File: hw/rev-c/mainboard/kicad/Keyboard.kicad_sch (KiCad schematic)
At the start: 7 parts, among them J15 KEYBOARD_EX, J5 KEYBOARD, U19 74LS145

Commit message: hw: fix wire/grid violations in schematic
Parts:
- J5: symbol Retrocomputing:CBM_PET_Keyboard_Conn_Keyed_20P -> EconoPET:CBM_PET_Keyboard_Conn_Keyed_20P
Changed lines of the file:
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@@
 	)
 	(symbol
-		(lib_id "Retrocomputing:CBM_PET_Keyboard_Conn_Keyed_20P")
+		(lib_id "EconoPET:CBM_PET_Keyboard_Conn_Keyed_20P")
 		(at 201.93 73.66 180)
 		(unit 1)

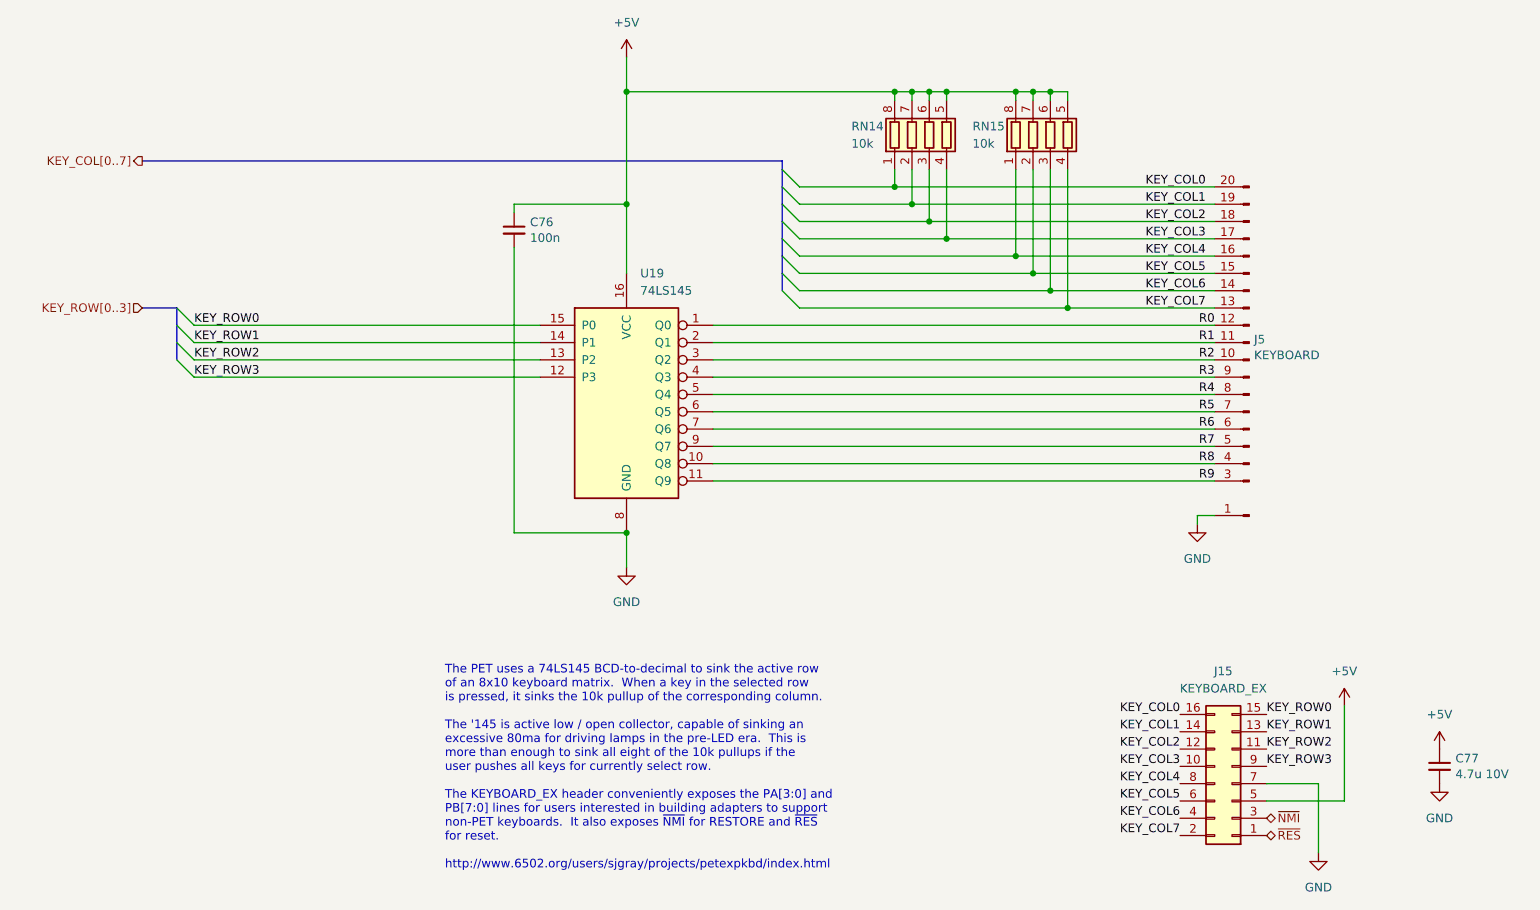
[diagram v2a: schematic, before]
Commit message: hw: renumber reference designators
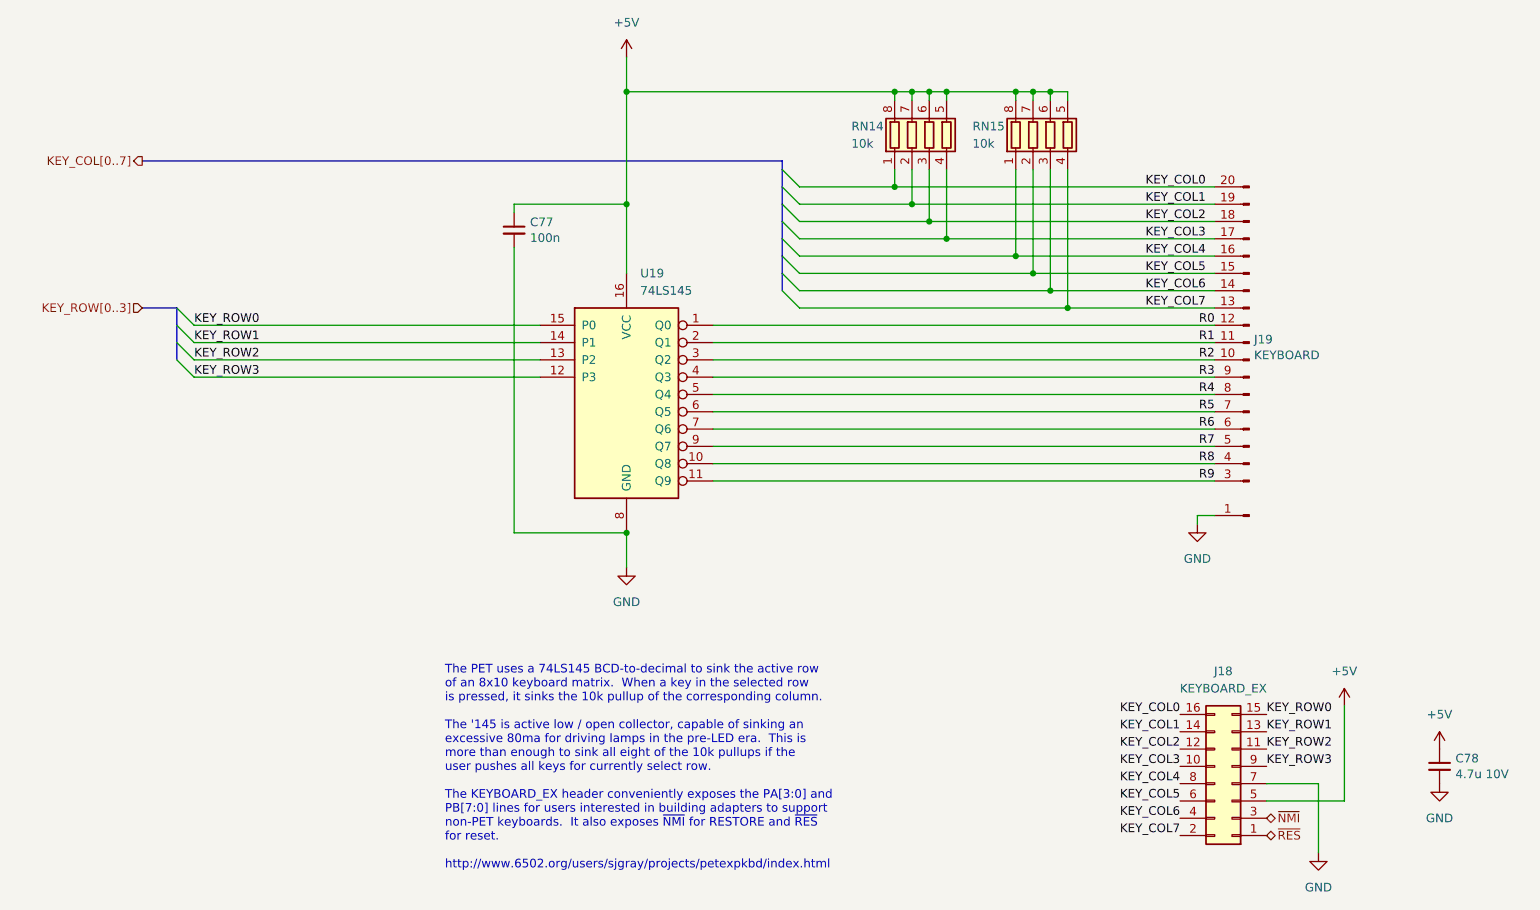
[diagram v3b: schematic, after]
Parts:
- renumbered C76 to C77, C77 to C78, J15 to J18, J5 to J19
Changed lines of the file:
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@@
 		(on_board yes)
 		(dnp no)
-		(property "Reference" "J5"
+		(property "Reference" "J19"
 			(at 202.6412 70.6628 0)
 			(effects
@@
 			(project ""
 				(path "/2eea20e6-112c-411a-b615-885ae773135a/00000000-0000-0000-0000-000061a7d9c6"
-					(reference "J5")
+					(reference "J19")
 					(unit 1)
 				)
@@
 		(on_board yes)
 		(dnp no)
-		(property "Reference" "C76"
+		(property "Reference" "C77"
 			(at 96.3168 53.4416 0)
 			(effects
@@
 			(project ""
 				(path "/2eea20e6-112c-411a-b615-885ae773135a/00000000-0000-0000-0000-000061a7d9c6"
-					(reference "C76")
+					(reference "C77")
 					(unit 1)
 				)
@@
 		(dnp no)
 		(fields_autoplaced yes)
-		(property "Reference" "#PWR0180"
+		(property "Reference" "#PWR0139"
 			(at 215.9 128.27 0)
 			(effects
@@
 			(project ""
 				(path "/2eea20e6-112c-411a-b615-885ae773135a/00000000-0000-0000-0000-000061a7d9c6"
-					(reference "#PWR0180")
+					(reference "#PWR0139")
 					(unit 1)
 				)
@@
 		(dnp no)
 		(fields_autoplaced yes)
-		(property "Reference" "J15"
+		(property "Reference" "J18"
 			(at 198.12 119.38 0)
 			(effects
@@
 			(project ""
 				(path "/2eea20e6-112c-411a-b615-885ae773135a/00000000-0000-0000-0000-000061a7d9c6"
-					(reference "J15")
+					(reference "J18")
 					(unit 1)
 				)
@@
 		(dnp no)
 		(fields_autoplaced yes)
-		(property "Reference" "#PWR0138"
+		(property "Reference" "#PWR0140"
 			(at 229.87 134.62 0)
 			(effects
@@
 			(project ""
 				(path "/2eea20e6-112c-411a-b615-885ae773135a/00000000-0000-0000-0000-000061a7d9c6"
-					(reference "#PWR0138")
+					(reference "#PWR0140")
 					(unit 1)
 				)
@@
 		(on_board yes)
 		(dnp no)
-		(property "Reference" "C77"
+		(property "Reference" "C78"
 			(at 232.2068 132.1816 0)
 			(effects
@@
 			(project ""
 				(path "/2eea20e6-112c-411a-b615-885ae773135a/00000000-0000-0000-0000-000061a7d9c6"
-					(reference "C77")
+					(reference "C78")
 					(unit 1)
 				)
@@
 		(dnp no)
 		(fields_autoplaced yes)
-		(property "Reference" "#PWR0179"
+		(property "Reference" "#PWR0138"
 			(at 212.09 152.4 0)
 			(effects
@@
 			(project ""
 				(path "/2eea20e6-112c-411a-b615-885ae773135a/00000000-0000-0000-0000-000061a7d9c6"
-					(reference "#PWR0179")
+					(reference "#PWR0138")
 					(unit 1)
 				)
@@
 		(dnp no)
 		(fields_autoplaced yes)
-		(property "Reference" "#PWR0139"
+		(property "Reference" "#PWR0141"
 			(at 229.87 142.24 0)
 			(effects
@@
 			(project ""
 				(path "/2eea20e6-112c-411a-b615-885ae773135a/00000000-0000-0000-0000-000061a7d9c6"
-					(reference "#PWR0139")
-					(unit 1)
-				)
+					(reference "#PWR0141")
+					(unit 1)
+				)

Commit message: hw: match original PET designators for connectors
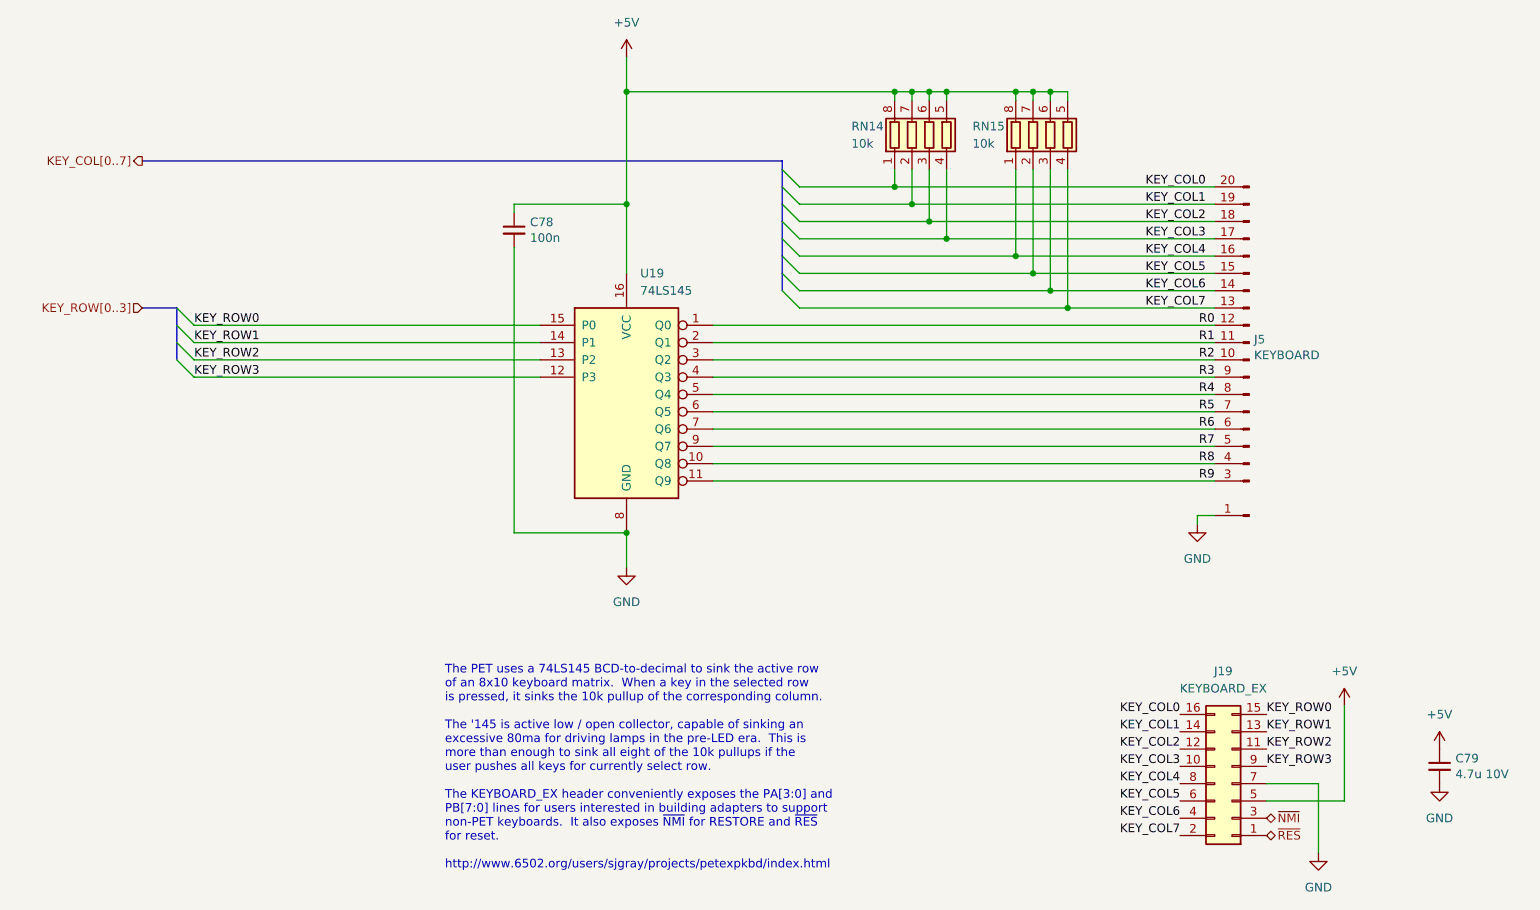
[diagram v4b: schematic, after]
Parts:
- renumbered C77 to C78, C78 to C79, J18 to J19, J19 to J5
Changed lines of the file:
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@@
 		(on_board yes)
 		(dnp no)
-		(property "Reference" "J19"
+		(property "Reference" "J5"
 			(at 202.6412 70.6628 0)
 			(effects
@@
 			(project ""
 				(path "/2eea20e6-112c-411a-b615-885ae773135a/00000000-0000-0000-0000-000061a7d9c6"
-					(reference "J19")
+					(reference "J5")
 					(unit 1)
 				)
@@
 		(on_board yes)
 		(dnp no)
-		(property "Reference" "C77"
+		(property "Reference" "C78"
 			(at 96.3168 53.4416 0)
 			(effects
@@
 			(project ""
 				(path "/2eea20e6-112c-411a-b615-885ae773135a/00000000-0000-0000-0000-000061a7d9c6"
-					(reference "C77")
+					(reference "C78")
 					(unit 1)
 				)
@@
 		(dnp no)
 		(fields_autoplaced yes)
-		(property "Reference" "J18"
+		(property "Reference" "J19"
 			(at 198.12 119.38 0)
 			(effects
@@
 			(project ""
 				(path "/2eea20e6-112c-411a-b615-885ae773135a/00000000-0000-0000-0000-000061a7d9c6"
-					(reference "J18")
+					(reference "J19")
 					(unit 1)
 				)
@@
 		(on_board yes)
 		(dnp no)
-		(property "Reference" "C78"
+		(property "Reference" "C79"
 			(at 232.2068 132.1816 0)
 			(effects
@@
 			(project ""
 				(path "/2eea20e6-112c-411a-b615-885ae773135a/00000000-0000-0000-0000-000061a7d9c6"
-					(reference "C78")
-					(unit 1)
-				)
+					(reference "C79")
+					(unit 1)
+				)

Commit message: hw: tidy warnings
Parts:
- J5: footprint Retrocomputing:CBM_PET_KEYBOARD_KEYED_20P -> EconoPET:CBM_PET_KEYBOARD_KEYED_20P
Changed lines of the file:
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@@
 			)
 		)
-		(property "Footprint" "Retrocomputing:CBM_PET_KEYBOARD_KEYED_20P"
+		(property "Footprint" "EconoPET:CBM_PET_KEYBOARD_KEYED_20P"
 			(at 201.93 73.66 0)
 			(effects

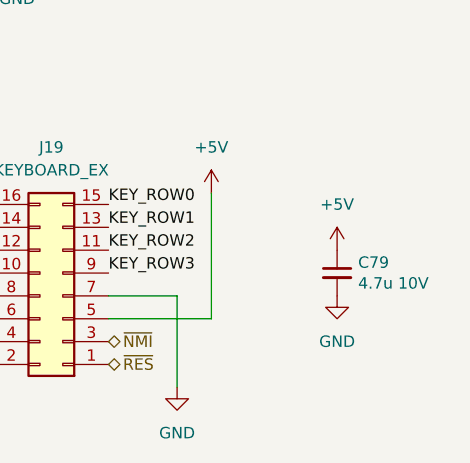
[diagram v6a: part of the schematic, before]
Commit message: hw: routing touchups, killer poke mitigation
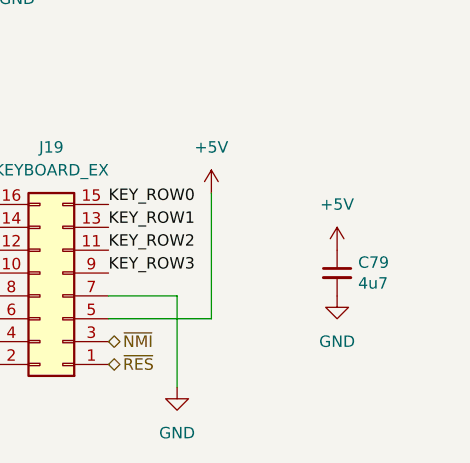
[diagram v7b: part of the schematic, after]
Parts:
- C79: value 4.7u 10V -> 4u7; LCSC C23733 -> C1538
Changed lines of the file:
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@@
 			)
 		)
-		(property "Value" "4.7u 10V"
+		(property "Value" "4u7"
 			(at 232.2068 134.493 0)
 			(effects
@@
 			)
 		)
-		(property "Datasheet" "https://product.samsungsem.com/mlcc/CL05A475MP5NRN.do"
+		(property "Datasheet" "https://www.lcsc.com/datasheet/lcsc_datasheet_2304140030_FH--Guangdong-Fenghua-Advanced-Tech-0402B472K500NT_C1538.pdf"
 			(at 229.87 133.35 0)
 			(effects
@@
 			)
 		)
-		(property "LCSC" "C23733"
+		(property "LCSC" "C1538"
 			(at 229.87 133.35 0)
 			(effects

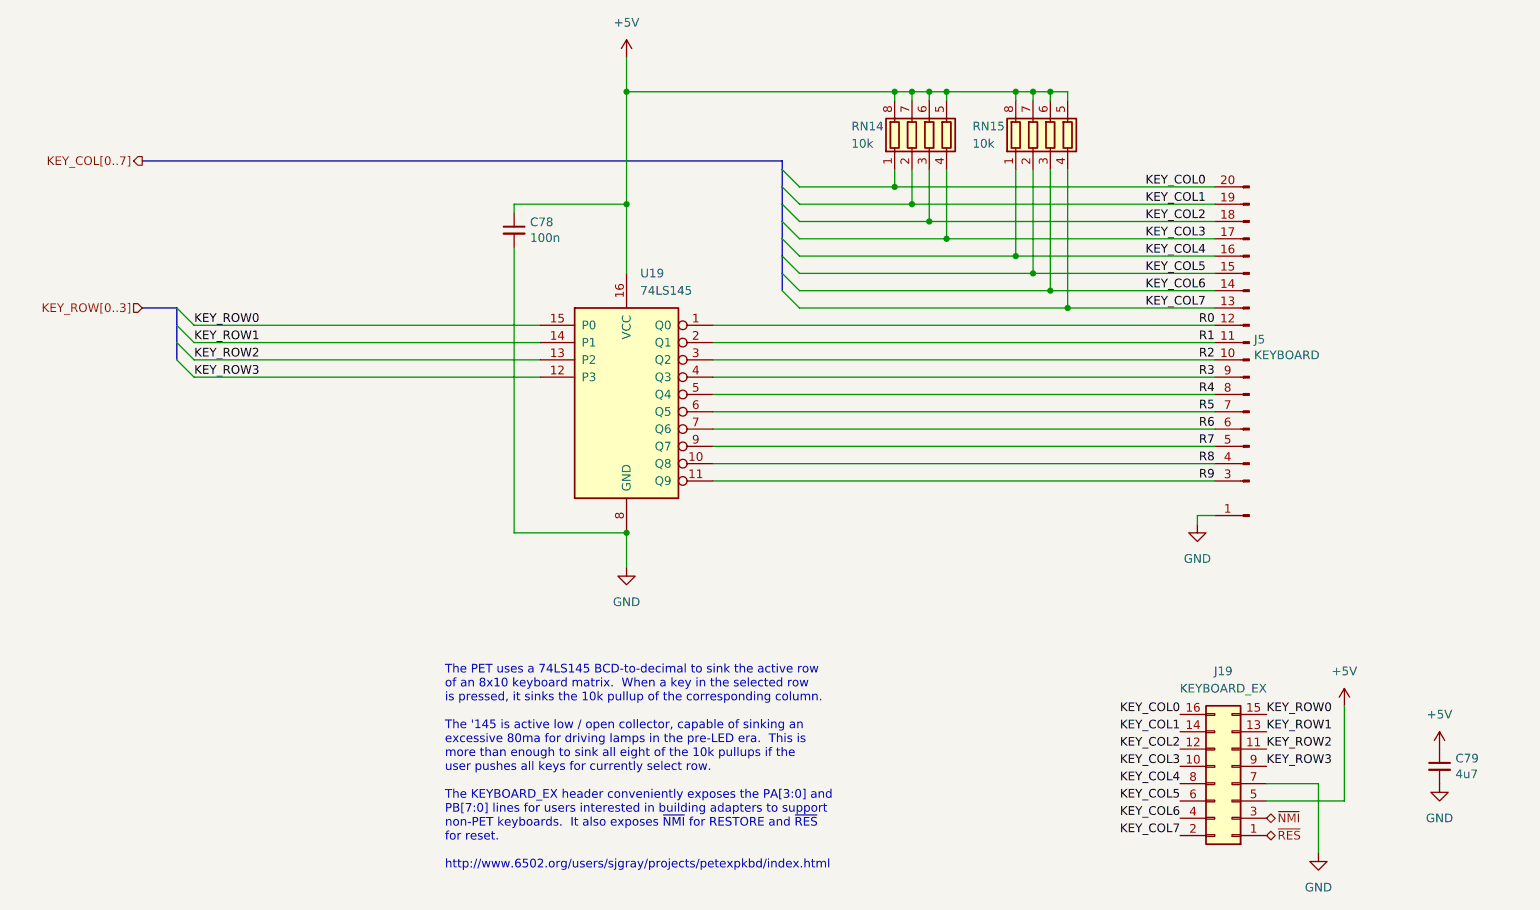
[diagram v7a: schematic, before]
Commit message: hw: fix/update parts / use parallel resistors to control 5V
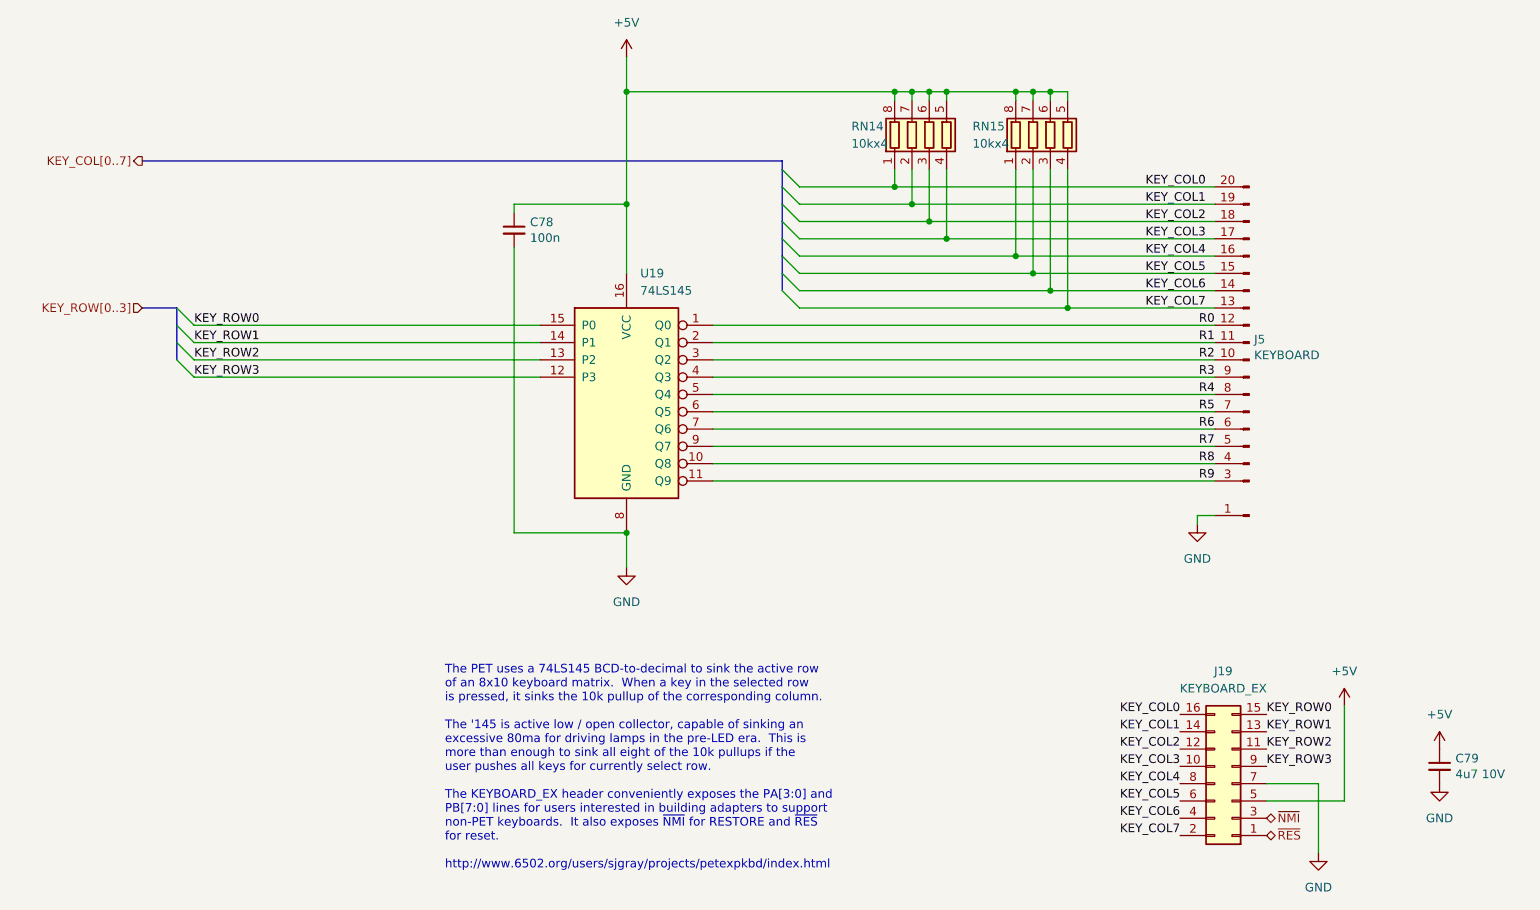
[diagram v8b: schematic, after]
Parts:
- C79: value 4u7 -> 4u7 10V; LCSC C1538 -> C23733
- RN14, RN15: value 10k -> 10kx4
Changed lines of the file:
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@@
 			)
 		)
-		(property "Datasheet" "https://datasheet.lcsc.com/lcsc/2304140030_Samsung-Electro-Mechanics-CL05B104KB54PNC_C307331.pdf"
+		(property "Datasheet" "https://product.samsungsem.com/mlcc/CL05B104KB54PN.do"
 			(at 93.98 54.61 0)
 			(effects
@@
 			)
 		)
-		(property "Datasheet" "https://datasheet.lcsc.com/lcsc/1809051911_Texas-Instruments-SN74LS145DR_C60829.pdf"
+		(property "Datasheet" "https://www.lcsc.com/datasheet/lcsc_datasheet_1809051911_Texas-Instruments-SN74LS145DR_C60829.pdf"
 			(at 110.49 78.74 0)
 			(effects
@@
 			)
 		)
-		(property "Value" "4u7"
+		(property "Value" "4u7 10V"
 			(at 232.2068 134.493 0)
 			(effects
@@
 			)
 		)
-		(property "Datasheet" "https://www.lcsc.com/datasheet/lcsc_datasheet_2304140030_FH--Guangdong-Fenghua-Advanced-Tech-0402B472K500NT_C1538.pdf"
+		(property "Datasheet" "https://product.samsungsem.com/mlcc/CL05A475MP5NRN.do"
 			(at 229.87 133.35 0)
 			(effects
@@
 			)
 		)
-		(property "LCSC" "C1538"
+		(property "LCSC" "C23733"
 			(at 229.87 133.35 0)
 			(effects
@@
 			)
 		)
-		(property "Value" "10k"
+		(property "Value" "10kx4"
 			(at 143.51 41.91 0)
 			(effects
@@
 			)
 		)
-		(property "Datasheet" "https://datasheet.lcsc.com/lcsc/2304140030_UNI-ROYAL-Uniroyal-Elec-4D03WGJ0103T5E_C29718.pdf"
+		(property "Datasheet" "https://www.lcsc.com/datasheet/lcsc_datasheet_2304140030_UNI-ROYAL-Uniroyal-Elec-4D03WGJ0103T5E_C29718.pdf"
 			(at 154.94 40.64 0)
 			(effects
@@
 			)
 		)
-		(property "Value" "10k"
+		(property "Value" "10kx4"
 			(at 161.29 41.91 0)
 			(effects
@@
 			)
 		)
-		(property "Datasheet" "https://datasheet.lcsc.com/lcsc/2304140030_UNI-ROYAL-Uniroyal-Elec-4D03WGJ0103T5E_C29718.pdf"
+		(property "Datasheet" "https://www.lcsc.com/datasheet/lcsc_datasheet_2304140030_UNI-ROYAL-Uniroyal-Elec-4D03WGJ0103T5E_C29718.pdf"
 			(at 172.72 40.64 0)
 			(effects
